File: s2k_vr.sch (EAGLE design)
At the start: 40 parts, among them IC1 74LS32D, Q1 12MHz

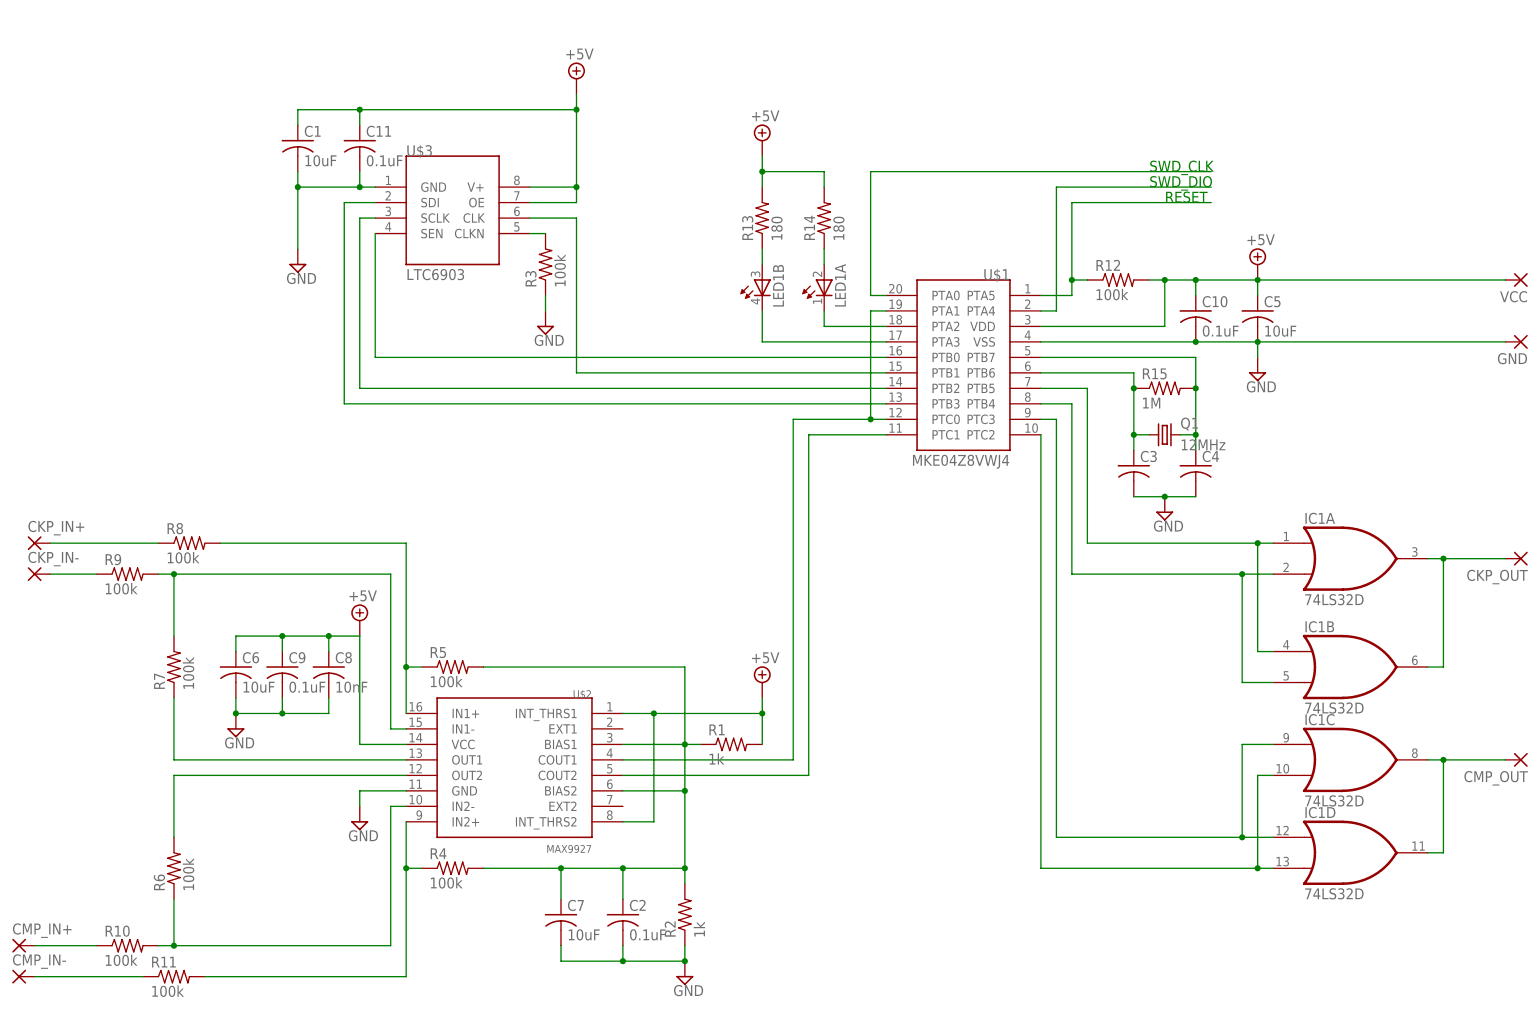
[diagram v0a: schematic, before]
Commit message: Add test pads and JTAG header
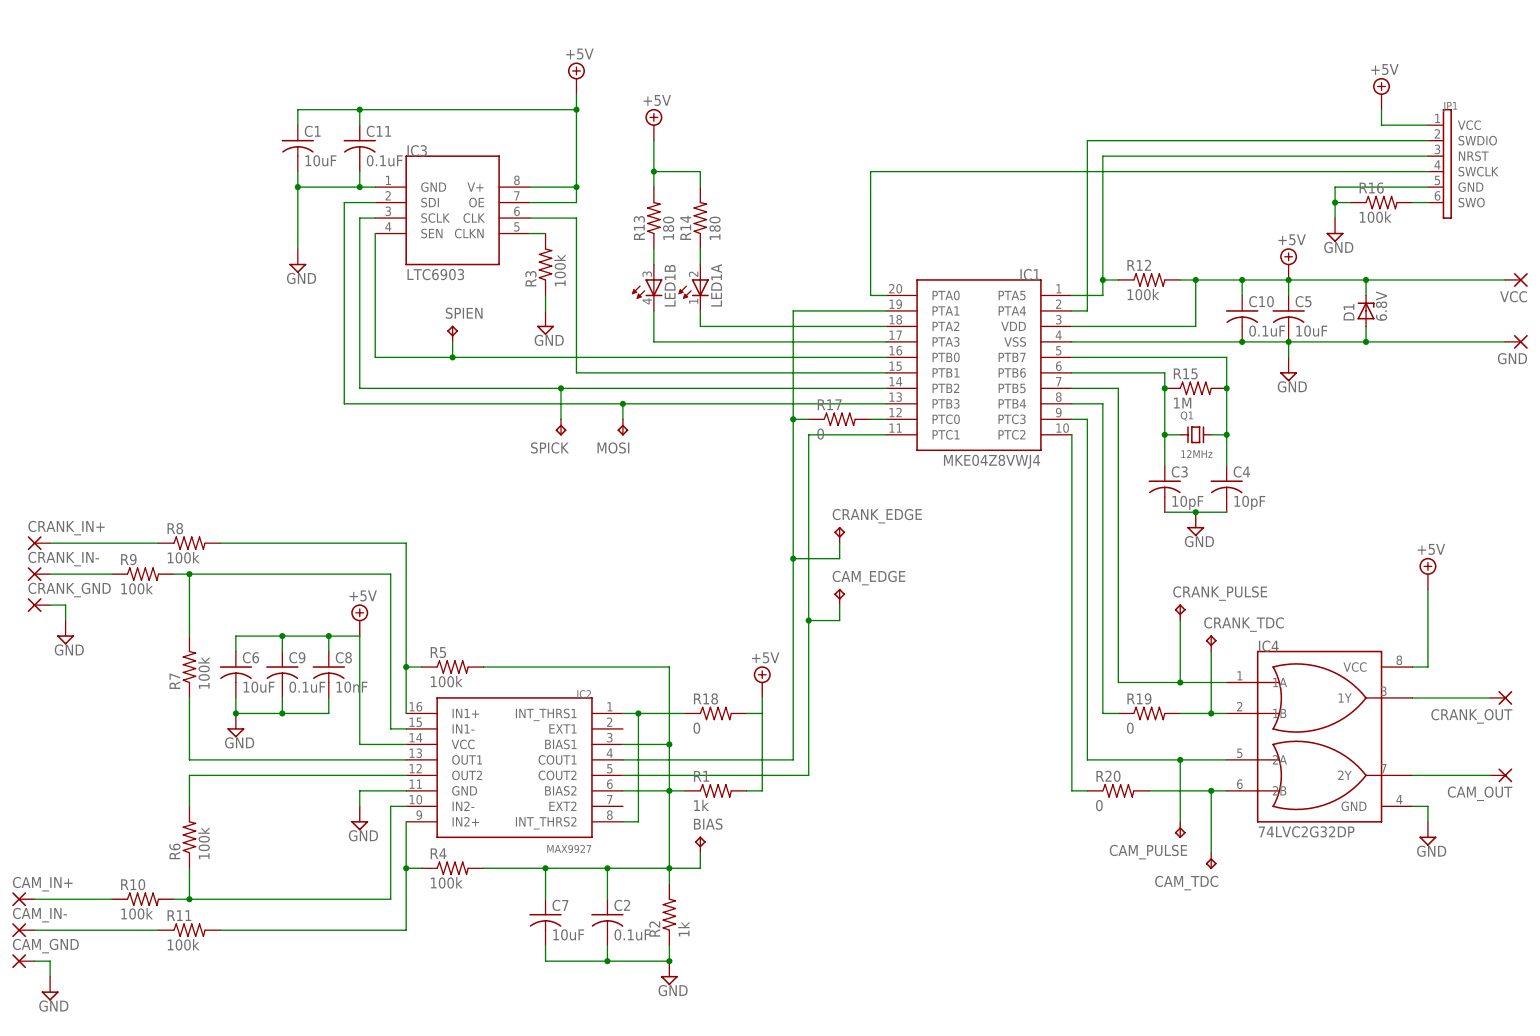
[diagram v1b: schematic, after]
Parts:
- removed CKP_OUT, CMP_IN+, CMP_IN-, CMP_OUT: (no value), wirepad:3,17/1,1
- removed U$1: MKE04Z8VWJ4, parts:MKE04Z8VWJ4
- added BIAS, CAM_EDGE, CAM_PULSE, CAM_TDC, CRANK_EDGE, CRANK_PULSE, CRANK_TDC, MOSI, SPICK, SPIEN: TPB2,54, testpad:TPB2,54
- added CAM_GND, CAM_IN+, CAM_IN-, CAM_OUT, CRANK_GND, CRANK_OUT: (no value), wirepad:3,17/1,1
- added D1: 6.8V, diode:ZENER-DIODESOT23
- added IC4: 74LVC2G32DP, parts:74LVC2G32DP
- added JP1: TC2030, parts:TC2030
- added R16: 100k, resistor:R-US_R0603
- added R17, R18, R19, R20: 0, resistor:R-US_R0603
- C3, C4: value (none) -> 10pF
- IC1: value 74LS32D -> MKE04Z8VWJ4; device 74xx-us:74LS32D -> parts:MKE04Z8VWJ4
- Q1: device crystal:CRYSTALHC49S -> parts:ABM10-167
- renumbered CKP_IN+ to CRANK_IN+, CKP_IN- to CRANK_IN-, U$2 to IC2, U$3 to IC3
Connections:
- new net N$25: JP1.SWO, R16.2
- new net N$35: IC1.PTC0, R17.2
- new net N$36: IC2.INT_THRS1, IC2.INT_THRS2, R18.1
- new net N$37: CRANK_TDC.TP, IC4.1B, R19.2
- new net N$38: CAM_TDC.TP, IC4.2B, R20.2
- net +5V: now also D1.C, IC1.VDD, IC4.VCC, JP1.VCC, R18.2; no longer IC2.INT_THRS1, IC2.INT_THRS2, U$1.VDD
- net GND: now also CAM_GND.P, CRANK_GND.P, D1.A, IC1.VSS, IC4.GND, JP1.GND, R16.1; no longer U$1.VSS
- net N$1: now also CRANK_EDGE.TP, IC1.PTA1, R17.1; no longer U$1.PTA1, U$1.PTC0
- net N$10: now also IC1.PTA4, JP1.SWDIO; no longer U$1.PTA4
- net N$11: now also IC1.PTA5, JP1.NRST; no longer U$1.PTA5
- net N$12: now also IC1.PTA3; no longer U$1.PTA3
- net N$14: now also IC1.PTB0, SPIEN.TP; no longer U$1.PTB0
- net N$15: now also IC1.PTB4, R19.1; no longer IC1A.I1, IC1B.I1, U$1.PTB4
- net N$16: now also CRANK_PULSE.TP, IC1.PTB5, IC4.1A; no longer IC1A.I0, IC1B.I0, U$1.PTB5
- net N$17: now also IC1.PTC2, R20.1; no longer IC1C.I1, IC1D.I1, U$1.PTC2
- net N$18: now also CAM_PULSE.TP, IC1.PTC3, IC4.2A; no longer IC1C.I0, IC1D.I0, U$1.PTC3
- net N$21: now also CRANK_OUT.P, IC4.1Y; no longer CKP_OUT.P, IC1A.O, IC1B.O
- net N$23: now also CAM_OUT.P, IC4.2Y; no longer CMP_OUT.P, IC1C.O, IC1D.O
- net N$26: now also IC1.PTB6; no longer U$1.PTB6
- net N$28: now also CAM_IN+.P; no longer CMP_IN+.P
- net N$29: now also CAM_IN-.P; no longer CMP_IN-.P
- net N$3: now also IC1.PTB2, SPICK.TP; no longer U$1.PTB2
- net N$30: now also IC1.PTB7; no longer U$1.PTB7
- net N$31: now also CAM_EDGE.TP, IC1.PTC1; no longer U$1.PTC1
- net N$4: now also IC1.PTB3, MOSI.TP; no longer U$1.PTB3
- net N$6: now also IC1.PTA2; no longer U$1.PTA2
- net N$7: now also IC1.PTB1; no longer U$1.PTB1
- net N$8: now also IC1.PTA0, JP1.SWCLK; no longer U$1.PTA0
- net N$9: now also BIAS.TP
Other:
- note removed: "RESET"
- note removed: "SWD_CLK"
- note removed: "SWD_DIO"
- moved on the sheet: C10, C2, C3, C4, C5, C7, LED1A, LED1B, R1, R10, R11, R12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

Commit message: Switch to MAX9926 and add output resistors
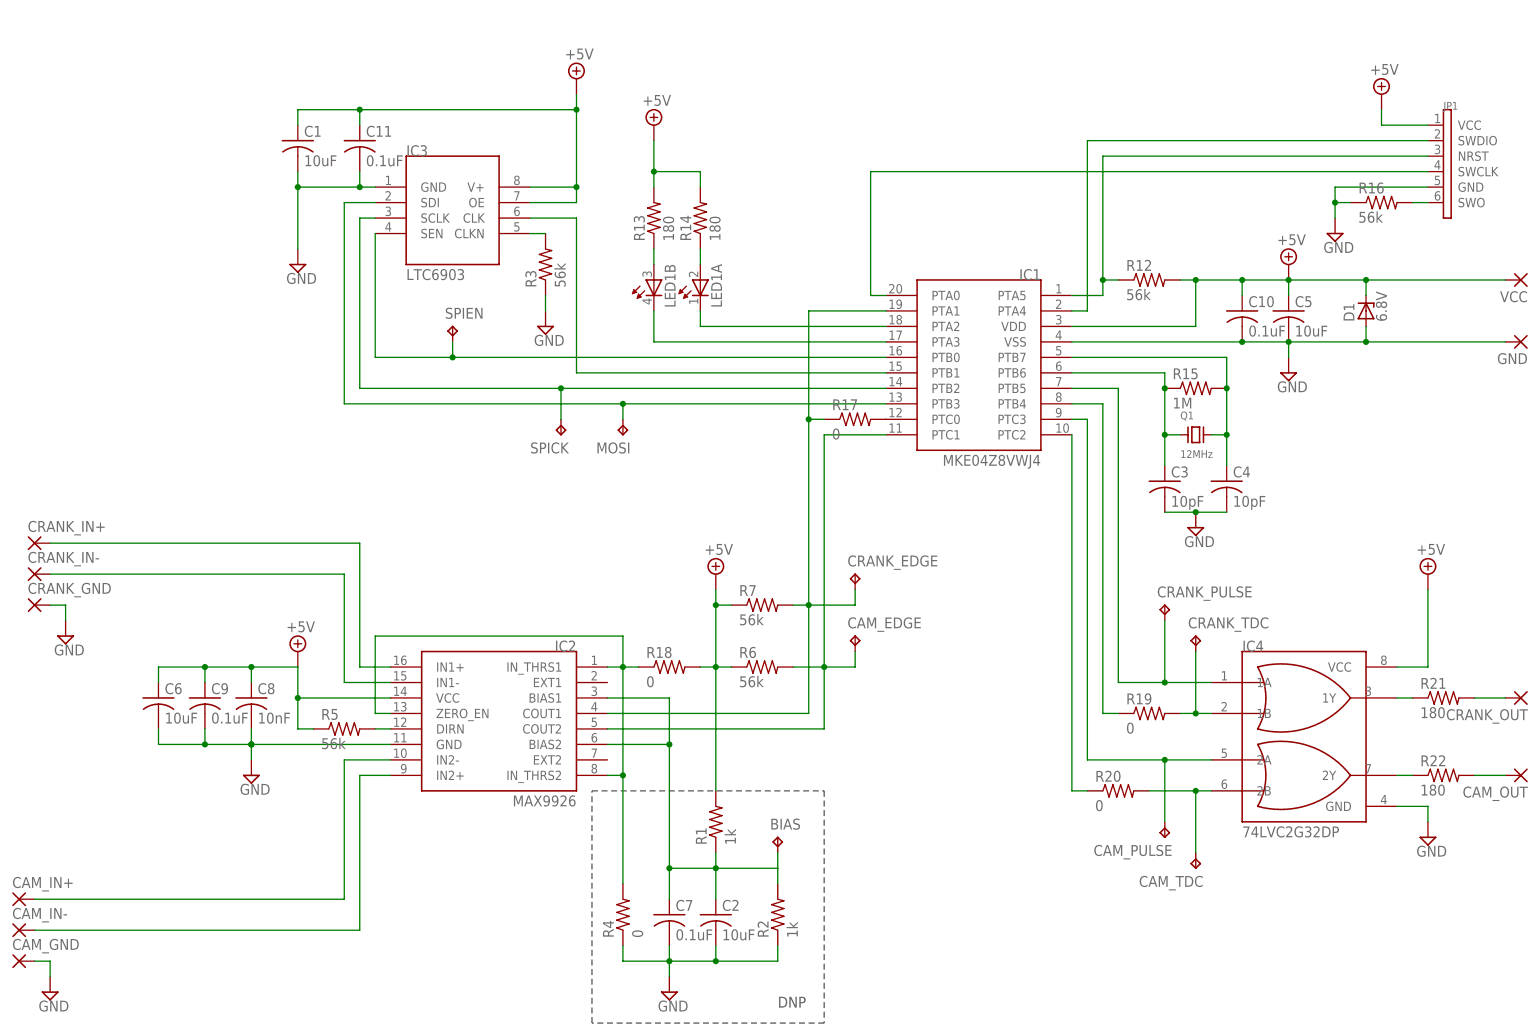
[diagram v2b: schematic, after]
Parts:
- removed R10, R11, R8, R9: 100k, resistor:R-US_R0603
- added R21, R22: 180, resistor:R-US_R0603
- C2: value 0.1uF -> 10uF
- C7: value 10uF -> 0.1uF
- IC2: value MAX9927 -> MAX9926; device parts:MAX9927 -> parts:MAX9926
- R12, R16, R3, R5, R6, R7: value 100k -> 56k
- R4: value 100k -> 0
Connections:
- removed net N$20: IC2.OUT2, R6.2
- removed net N$22: CRANK_IN-.P, R9.1
- removed net N$28: CAM_IN+.P, R10.1
- removed net N$29: CAM_IN-.P, R11.1
- removed net N$9: BIAS.TP, C2.1, C7.1, IC2.BIAS1, IC2.BIAS2, R1.1, R2.2, R4.2, R5.2
- new net N$39: IC4.2Y, R22.1
- new net N$40: CAM_OUT.P, R22.2
- net +5V: now also R5.1, R6.1, R7.1
- net GND: now also R4.1
- net N$1: now also R7.2
- net N$19: now also BIAS.TP, C2.1, C7.1, IC2.BIAS1, IC2.BIAS2, R1.1, R2.2; no longer IC2.OUT1, R7.1
- net N$2: now also CAM_IN-.P; no longer R11.2, R4.1
- net N$21: now also R21.1; no longer CRANK_OUT.P
- net N$23: now also CRANK_OUT.P, R21.2; no longer CAM_OUT.P, IC4.2Y
- net N$24: now also IC2.IN1+; no longer R8.1
- net N$27: now also CAM_IN+.P; no longer R10.2, R6.1
- net N$31: now also R6.2
- net N$34: now also CRANK_IN-.P; no longer R7.2, R9.2
- net N$36: now also IC2.IN_THRS1, IC2.IN_THRS2, IC2.ZERO_EN, R4.2; no longer IC2.INT_THRS1, IC2.INT_THRS2
- net N$5: now also IC2.DIRN, R5.2; no longer IC2.IN1+, R5.1, R8.2
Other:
- note added: "DNP"
- moved on the sheet: BIAS, C2, C6, C7, C8, C9, CAM_EDGE, CAM_OUT, CAM_PULSE, CAM_TDC, CRANK_EDGE, CRANK_OUT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

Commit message: Use Lite-On RGB LED
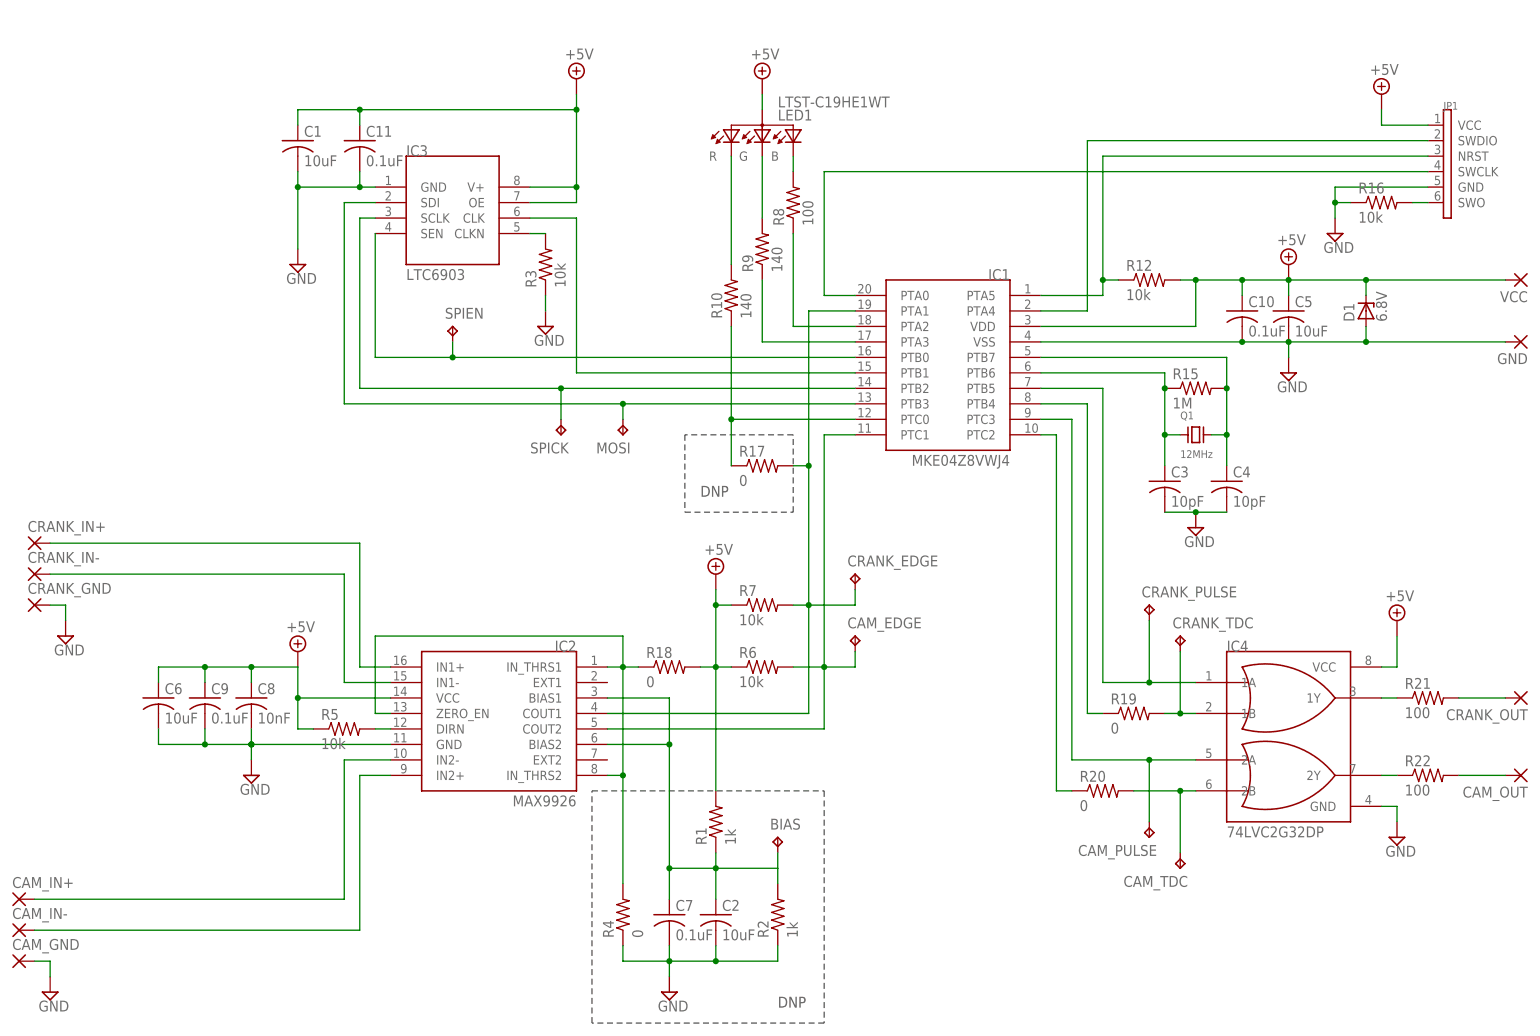
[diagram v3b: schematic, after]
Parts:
- removed R13, R14: 180, resistor:R-US_R0603
- added R10, R9: 140, resistor:R-US_R0603
- added R8: 100, resistor:R-US_R0603
- C1, C5, C6: device resistor:C-USC0603 -> resistor:C-USC0805
- C8: device resistor:C-USC0603 -> parts:CAP-0306
- LED1: value (none) -> LTST-C19HE1WT; device led:TOPLED-2-- -> parts:LTST-C19HE1WT
- R12, R16, R3, R5, R6, R7: value 56k -> 10k
- R21, R22: value 180 -> 100
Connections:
- removed net N$32: LED1A.A, R14.1
- removed net N$33: LED1B.A, R13.1
- removed net N$35: IC1.PTC0, R17.2
- new net N$20: LED1.G, R9.2
- new net N$22: LED1.R, R10.2
- new net N$28: IC1.PTC0, R10.1, R17.1
- new net N$9: LED1.B, R8.2
- net +5V: now also LED1.ANODE; no longer R13.2, R14.2
- net N$1: now also R17.2; no longer R17.1
- net N$12: now also R9.1; no longer LED1B.C
- net N$6: now also R8.1; no longer LED1A.C
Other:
- moved on the sheet: CAM_PULSE, CAM_TDC, CRANK_PULSE, CRANK_TDC, IC1, IC4, R17, R19, R20, R21, R22
